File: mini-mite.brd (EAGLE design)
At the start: 38.6 x 34 mm, 27 parts, among them IC2 LM7805, Q1 2N2222, Q2 2N2907, Q3 IRF2804, Q4 IRF2804, U1 ATTiny13

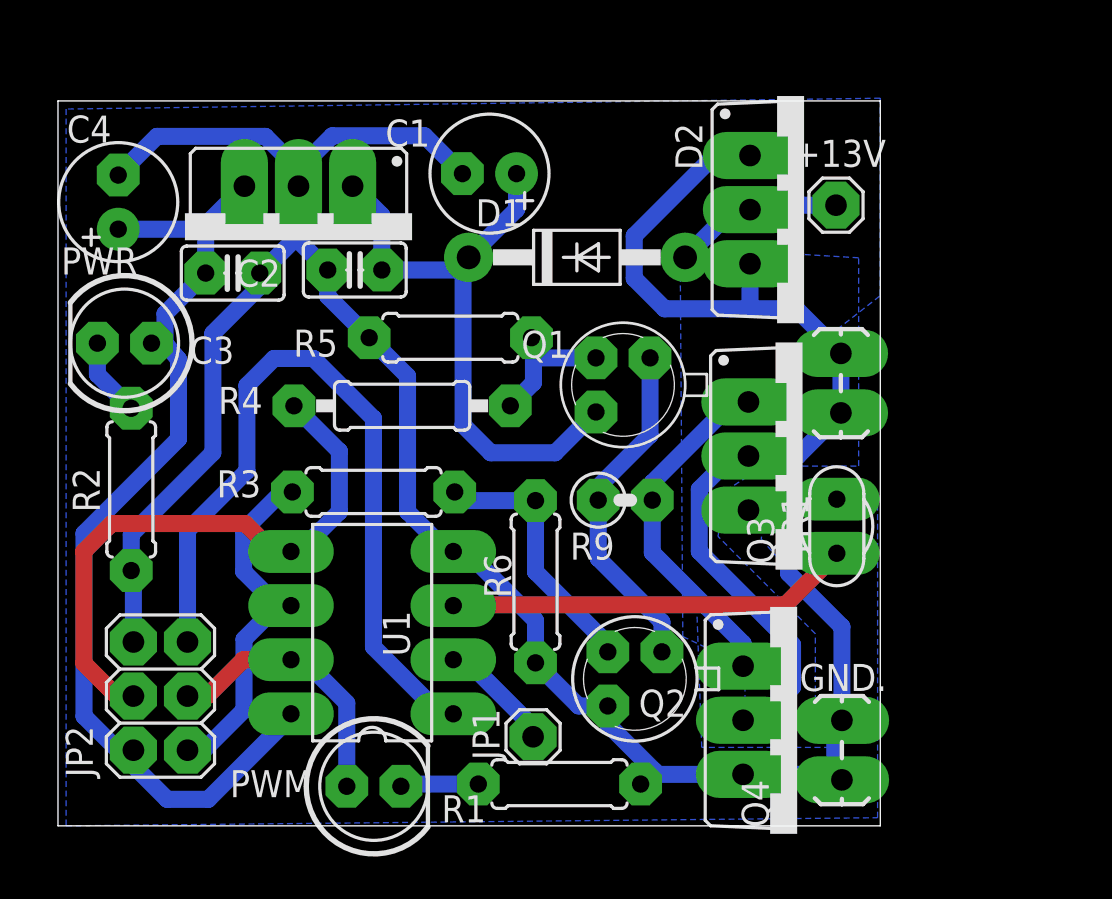
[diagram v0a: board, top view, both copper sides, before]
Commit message: Fixed drive voltage range bug.
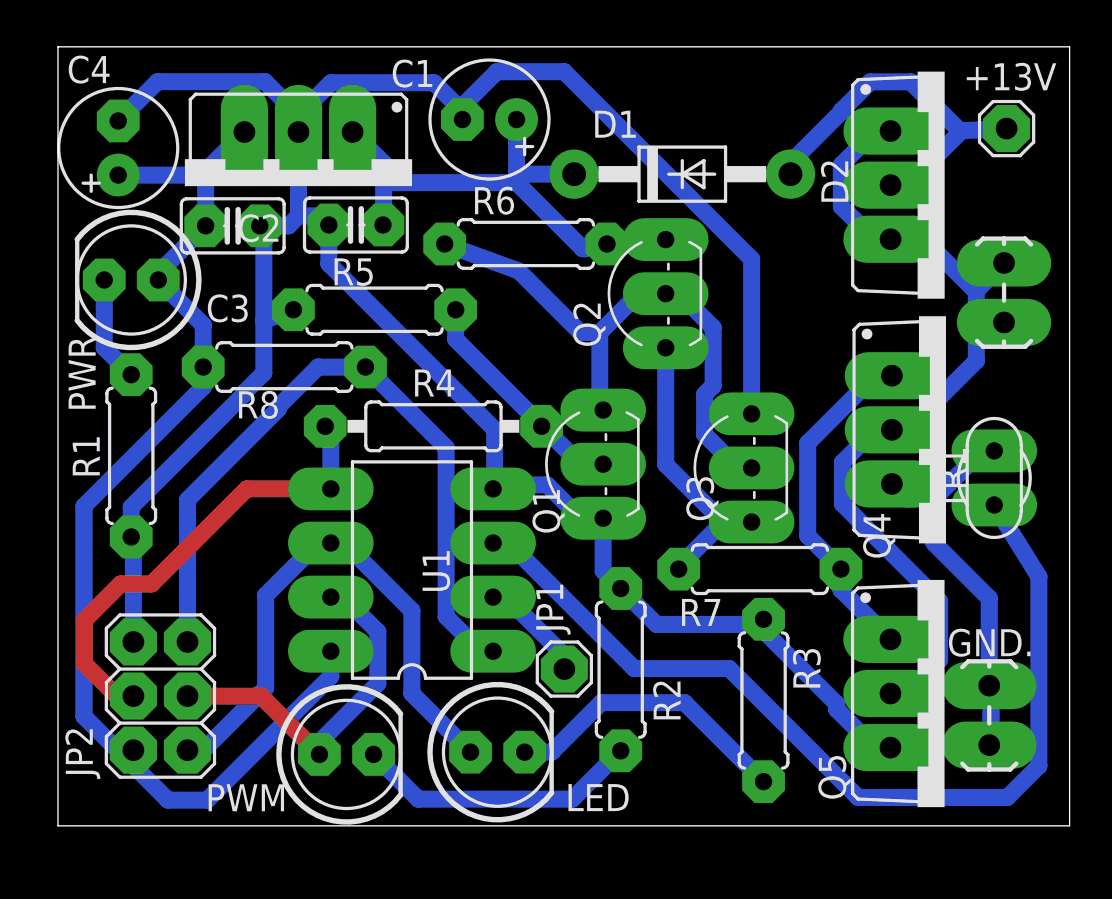
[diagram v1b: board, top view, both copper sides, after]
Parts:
- removed R9: 10, resistor:0207/2V
- added LED: yellow, led:LED5MM
- added Q5: IRF2804, transistor-power:TO220BV
- added R7: 10, resistor:0207/7
- added R8: 10k, resistor:0207/7
- D2: value DI_MBR2060CT -> MBR2060CT
- PWR: value (none) -> red
- Q1: device transistor:TO18 -> adafruit:TO92-EBC-OVAL
- Q2: value 2N2907 -> 2N2222; device transistor-pnp:TO18 -> adafruit:TO92-EBC-OVAL
- Q3: value IRF2804 -> 2N2907; device transistor-power:TO220BV -> adafruit:TO92-EBC-OVAL
- R3: value 47 -> 1K
- moved R1 25.3 mm to (3.44, 17.4), turned to 90 degrees
- moved R2 24.5 mm to (26.4, 7.33), turned to 270 degrees
- moved R3 20.8 mm to (33.1, 5.89), turned to 270 degrees
- moved Q2 18.1 mm to (27.3, 25.0), turned to 90 degrees
- moved R6 15.9 mm to (22.0, 27.3), turned to 0 degrees
- moved Q4 15.3 mm to (41.7, 18.6)
- moved +13V 8.78 mm to (44.5, 32.7)
- moved M- 8.76 mm to (44.4, 26.3)
- moved TR1 7.73 mm to (44.0, 16.3)
- moved GND. 7.11 mm to (43.7, 6.46)
- moved D2 6.70 mm to (41.6, 30.1)
- moved D1 6.31 mm to (29.3, 30.6)
- moved Q1 4.32 mm to (24.3, 17.0), turned to 90 degrees
- moved R5 3.79 mm to (14.9, 24.2)
- moved Q3 3.70 mm to (31.3, 16.8), turned to 90 degrees
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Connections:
- removed net GATECTL: Q1.2, R4.2, R5.2
- removed net GATEDRV: Q3.G, Q4.G, R9.2
- removed net LOGATECTL: Q2.2, R3.2, R6.2
- removed net N$3: Q1.1, Q2.1, R9.1
- new net GATEON: Q1.C, Q2.B, Q3.B, R6.1
- new net GATE_DRV: Q4.G, Q5.G, R7.2
- new net N$1: LED.K, R3.2
- new net N$4: Q2.E, Q3.E, R7.1
- new net ~GATE_ON: Q1.B, R4.2, R5.2
- net 12V: now also Q2.C, R6.2; no longer Q1.3
- net GND: now also Q1.E, Q3.C, Q5.S, R3.1; no longer Q2.3, Q3.S, R6.1
- net M-: now also Q5.D; no longer Q3.D
- net MISO: now also LED.A; no longer R3.1
- net N$19: now also R2.2; no longer R1.2
- net N$5: now also R1.2; no longer R2.2
- net RESET: now also R8.2
- net VCC: now also R8.1
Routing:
- net GND: track 105.5 -> 141.2 mm
- net GATEON: track 0.00 -> 27.2 mm
- net ADC2: track 19.0 -> 44.0 mm
- net GATEDRV: track 16.5 -> 0.00 mm
- net GATE_DRV: track 0.00 -> 16.1 mm
- net N$3: track 16.1 -> 0.00 mm
- net N$1: track 0.00 -> 13.7 mm
- net N$4: track 0.00 -> 13.7 mm
- net LOGATECTL: track 12.5 -> 0.00 mm
- net ~GATE_ON: track 0.00 -> 10.8 mm
- net N$19: track 3.68 -> 13.4 mm
- net +13V: track 8.10 -> 17.6 mm
- net MISO: track 16.8 -> 26.2 mm
- net VCC: track 46.7 -> 53.6 mm
- net GATECTL: track 6.62 -> 0.00 mm
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- removed copper zone on layer 16, net GND
- removed copper zone on layer 16, net M-
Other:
- board size 38.6 x 34 mm -> 47.5 x 36.6 mm
